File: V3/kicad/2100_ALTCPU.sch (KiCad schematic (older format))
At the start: 7 parts, among them J2100 Conn_02x20_Counter_Clockwise, U2100 Z8-L180-S180-180-PQFP-80, U2101 GAL16V8, X2100 14.7456 MHz

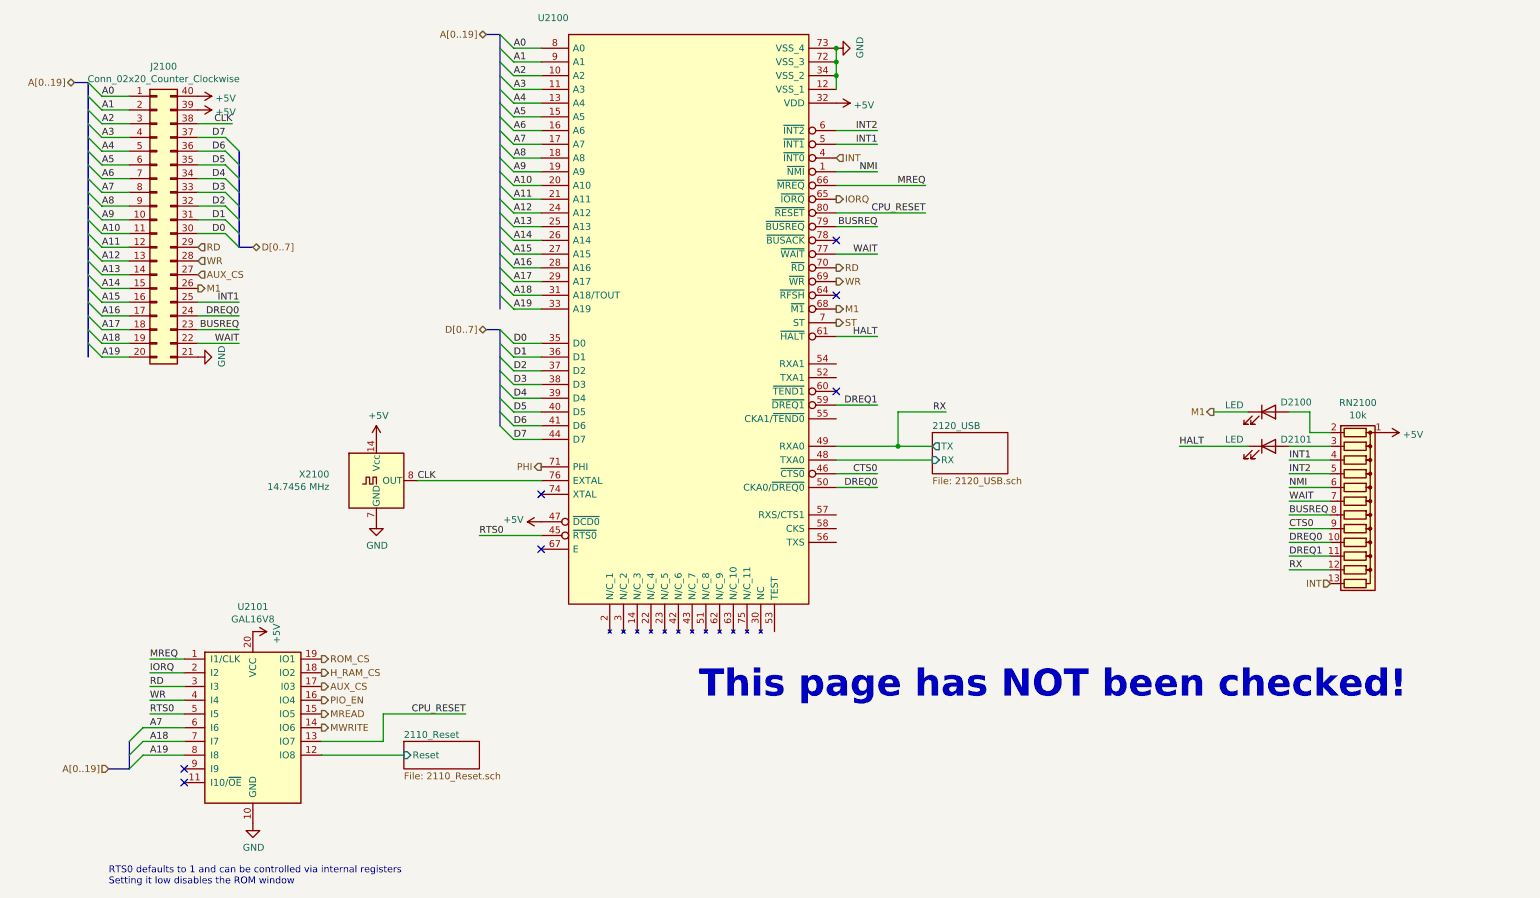
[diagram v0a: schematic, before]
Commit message: Fixed a few USB/UART issues
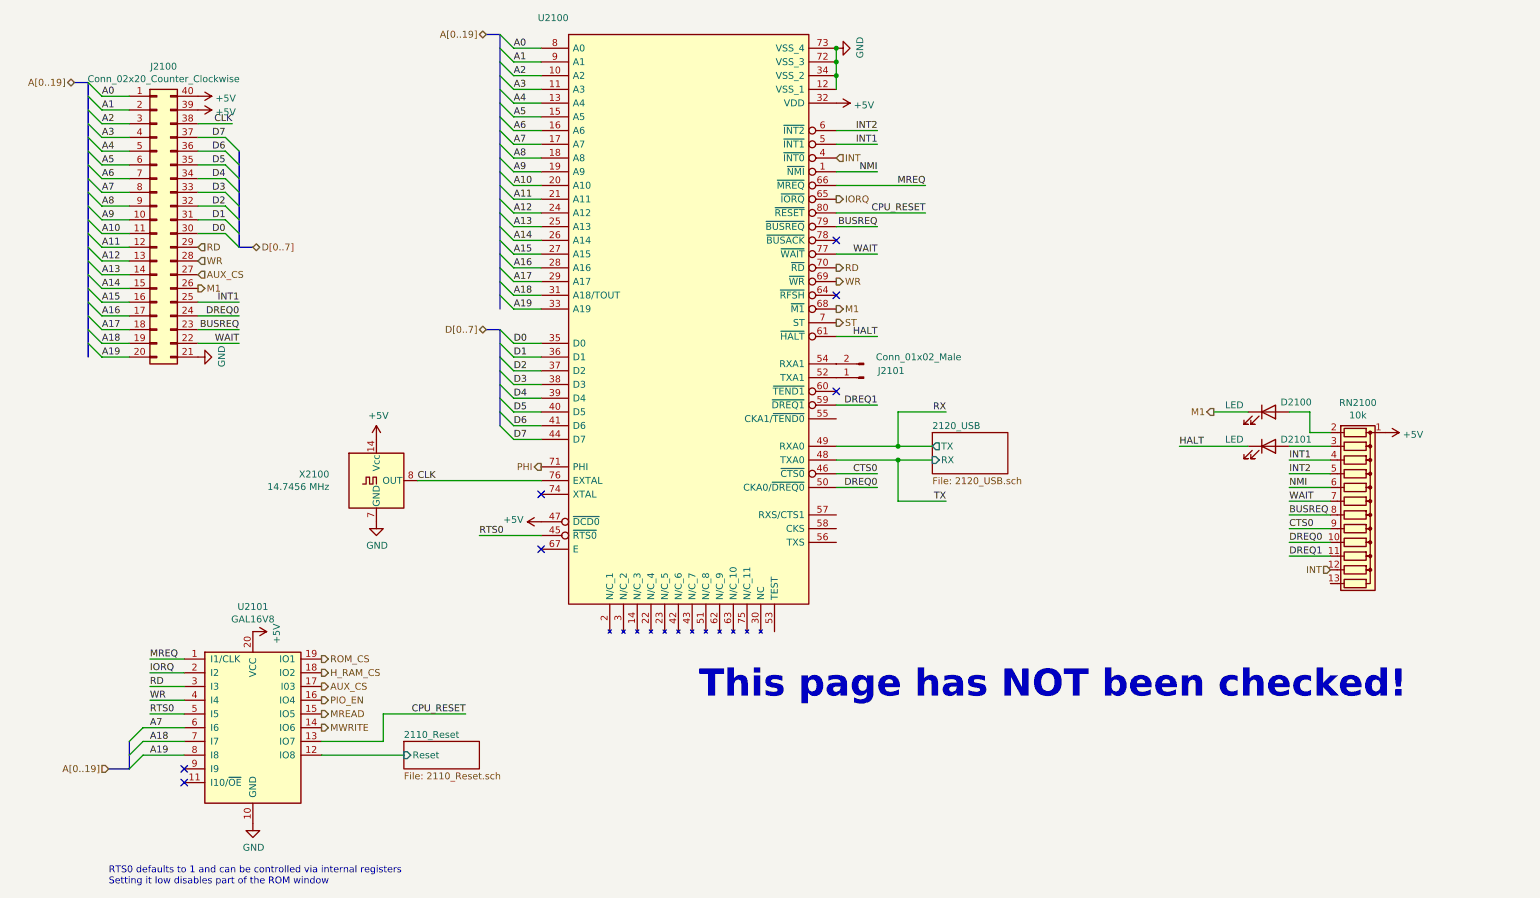
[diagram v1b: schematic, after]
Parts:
- added J2101: Conn_01x02_Male, Connector_PinHeader_2.54mm:PinHeader_1x02_P2.54mm_Vertical, symbol Connector:Conn_01x02_Male
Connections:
- net INT: now also RN2100.12 (R11); no longer RN2100.13 (R12)
- net RX: no longer RN2100.12 (R11)
- net at U2100.52 (TXA1): now also J2101.1 (Pin_1)
- net at U2100.54 (RXA1): now also J2101.2 (Pin_2)
- net 2120_USB/RX renamed TX
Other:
- note added: "RTS0 defaults to 1 and can be controlled via internal registers\nSetting it low disables part of the ROM window"
- note removed: "RTS0 defaults to 1 and can be controlled via internal registers\nSetting it low disables the ROM window"
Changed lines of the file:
@@
 Text HLabel 9500 4150 0    50   Output ~ 0
 M1
-Text HLabel 10350 5400 0    50   Input ~ 0
+Text HLabel 10350 5300 0    50   Input ~ 0
 INT
 NoConn ~ 6750 4000
@@
 	2000 6350 1750 6350
 Text Notes 1450 7600 0    50   ~ 0
-RTS0 defaults to 1 and can be controlled via internal registers\nSetting it low disables the ROM window
+RTS0 defaults to 1 and can be controlled via internal registers\nSetting it low disables part of the ROM window
 Wire Wire Line
 	3600 6650 3000 6650
@@
 	3700 4650 4600 4650
 Wire Wire Line
-	6750 4500 7450 4500
+	6750 4500 7200 4500
 NoConn ~ 2000 6750
 $Comp
@@
 Text Label 7550 4150 2    50   ~ 0
 RX
-Text Label 10050 5300 0    50   ~ 0
-RX
-Wire Wire Line
-	10350 5300 10050 5300
 Wire Wire Line
 	6750 4100 7050 4100
@@
 DREQ0
 $Comp
-L power:GND #PWR?
+L power:GND #PWR0140
 U 1 1 6275CB20
 P 2100 3750
-F 0 "#PWR?" H 2100 3500 50  0001 C CNN
+F 0 "#PWR0140" H 2100 3500 50  0001 C CNN
 F 1 "GND" H 2105 3577 50  0000 C CNN
 F 2 "" H 2100 3750 50  0001 C CNN
@@
 $EndComp
 $Comp
-L power:+5V #PWR?
+L power:+5V #PWR0142
 U 1 1 6275CB26
 P 2100 1850
-F 0 "#PWR?" H 2100 1700 50  0001 C CNN
+F 0 "#PWR0142" H 2100 1700 50  0001 C CNN
 F 1 "+5V" V 2115 1978 50  0000 L CNN
 F 2 "" H 2100 1850 50  0001 C CNN
@@
 $EndComp
 $Comp
-L power:+5V #PWR?
+L power:+5V #PWR0144
 U 1 1 627A29E2
 P 2100 1950
-F 0 "#PWR?" H 2100 1800 50  0001 C CNN
+F 0 "#PWR0144" H 2100 1800 50  0001 C CNN
 F 1 "+5V" V 2115 2078 50  0000 L CNN
 F 2 "" H 2100 1950 50  0001 C CNN
@@
 	0    1    1    0
 $EndComp
+Wire Wire Line
+	7200 4800 7550 4800
+Text Label 7550 4800 2    50   ~ 0
+TX
+Connection ~ 7200 4500
+Wire Wire Line
+	7200 4500 7450 4500
+Wire Wire Line
+	7200 4500 7200 4800
+$Comp
+L Connector:Conn_01x02_Male J?
+U 1 1 62765282
+P 6950 3900
+AR Path="/6191B6A2/61EBDADB/62542978/62765282" Ref="J?"  Part="1"
+AR Path="/6191B6A2/61EBDADB/62765282" Ref="J2101"  Part="1"
+F 0 "J2101" H 6750 3850 50  0000 C CNN
+F 1 "Conn_01x02_Male" H 6550 3750 50  0000 C CNN
+F 2 "Connector_PinHeader_2.54mm:PinHeader_1x02_P2.54mm_Vertical" H 6950 3900 50  0001 C CNN
+F 3 "~" H 6950 3900 50  0001 C CNN
+	1    6950 3900
+	-1   0    0    1
+$EndComp
 Wire Bus Line

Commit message: Still putting final touches on CPU page
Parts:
- removed J2100: Conn_02x20_Counter_Clockwise, Connector_PinSocket_2.54mm:PinSocket_2x20_P2.54mm_Vertical, symbol Connector_Generic:Conn_02x20_Counter_Clockwise
- removed RN2100: 10k, Resistor_THT:R_Array_SIP13, symbol Device:R_Network12
- added D2102: LED, LED_THT:LED_D3.0mm, symbol Device:LED
- added J2100: Conn_02x24_Counter_Clockwise, Connector_PinSocket_2.54mm:PinSocket_2x24_P2.54mm_Vertical, symbol Connector_Generic:Conn_02x24_Counter_Clockwise
- added RN2100: 10k, Resistor_THT:R_Array_SIP14, symbol Device:R_Network13
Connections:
- net +5V: now also J2100.23 (Pin_23), J2100.24 (Pin_24), RN2100.1 (common); no longer U2100.47 (~DCD0)
- net A0: now also J2100.1 (Pin_1)
- net A1: now also J2100.2 (Pin_2)
- net A10: now also J2100.11 (Pin_11)
- net A11: now also J2100.12 (Pin_12)
- net A12: now also J2100.13 (Pin_13)
- net A13: now also J2100.14 (Pin_14)
- net A14: now also J2100.15 (Pin_15)
- net A15: now also J2100.16 (Pin_16)
- net A16: now also J2100.17 (Pin_17)
- net A17: now also J2100.18 (Pin_18)
- net A18: now also J2100.19 (Pin_19)
- net A19: now also J2100.20 (Pin_20)
- net A2: now also J2100.3 (Pin_3)
- net A3: now also J2100.4 (Pin_4)
- net A4: now also J2100.5 (Pin_5)
- net A5: now also J2100.6 (Pin_6)
- net A6: now also J2100.7 (Pin_7)
- net A7: now also J2100.8 (Pin_8)
- net A8: now also J2100.9 (Pin_9)
- net A9: now also J2100.10 (Pin_10)
- net AUX_CS: now also J2100.38 (Pin_38)
- net BUSREQ: now also J2100.32 (Pin_32), RN2100.10 (R9)
- net CTS0: now also RN2100.11 (R10)
- net D0: now also J2100.41 (Pin_41)
- net D1: now also J2100.42 (Pin_42)
- net D2: now also J2100.43 (Pin_43)
- net D3: now also J2100.44 (Pin_44)
- net D4: now also J2100.45 (Pin_45)
- net D5: now also J2100.46 (Pin_46)
- net D6: now also J2100.47 (Pin_47)
- net D7: now also J2100.48 (Pin_48)
- net DREQ0: now also J2100.33 (Pin_33); no longer U2100.50 (CKA0/~DREQ0)
- net DREQ1: now also RN2100.13 (R12)
- net GND: now also D2102.1 (K), J2100.25 (Pin_25), J2100.26 (Pin_26)
- net INT: now also RN2100.5 (R4)
- net INT1: now also J2100.34 (Pin_34), RN2100.6 (R5)
- net INT2: now also RN2100.7 (R6)
- net IORQ: now also J2100.30 (Pin_30)
- net M1: now also J2100.40 (Pin_40)
- net MREQ: now also J2100.29 (Pin_29)
- net NMI: now also RN2100.8 (R7)
- net PHI: now also J2100.39 (Pin_39)
- net RD: now also J2100.35 (Pin_35)
- net RTS0: now also J2100.28 (Pin_28)
- net WAIT: now also J2100.31 (Pin_31), RN2100.9 (R8)
- net WR: now also J2100.36 (Pin_36)
- net RXS: now reaches U2100.57 (RXS/CTS1)
- net RXS: now also RN2100.12 (R11)
- net at D2101.2 (A): now also RN2100.3 (R2)
- net at D2100.2 (A): now also RN2100.2 (R1)
- net CPU_RESET renamed C_RST
- net C_RST: now also J2100.27 (Pin_27)
- net ST: no longer names the net of U2100.7 (ST)
- new net: D2102.2 (A), RN2100.4 (R3)
- new net DCD0: RN2100.14 (R13), U2100.47 (~DCD0)
- no-connect marks 7 -> 13
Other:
- note added: "Tie CKS high?"
- moved on the sheet: D2100, D2101

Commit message: Hopefully the last major changes to the CPU
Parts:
- removed D2102: LED, LED_THT:LED_D3.0mm, symbol Device:LED
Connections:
- net 2110_Reset/Reset: now also U2101.9 (I9); no longer U2101.12 (IO8)
- net AUX_CS: now also J2100.21 (Pin_21); no longer J2100.38 (Pin_38)
- net BUSREQ: now also RN2100.9 (R8); no longer RN2100.10 (R9)
- net CTS0: now also RN2100.10 (R9); no longer RN2100.11 (R10)
- net C_RST: now also U2101.12 (IO8); no longer U2101.13 (IO7)
- net DCD0: now also RN2100.13 (R12); no longer RN2100.14 (R13)
- net DREQ1: now also RN2100.12 (R11); no longer RN2100.13 (R12)
- net INT: now also RN2100.4 (R3); no longer RN2100.5 (R4)
- net INT1: now also RN2100.5 (R4); no longer RN2100.6 (R5)
- net INT2: now also RN2100.6 (R5); no longer RN2100.7 (R6)
- net M1: now also J2100.37 (Pin_37); no longer J2100.40 (Pin_40)
- net NMI: now also RN2100.7 (R6); no longer RN2100.8 (R7)
- net PHI: now also J2100.38 (Pin_38); no longer J2100.39 (Pin_39)
- net RXS: now also RN2100.11 (R10); no longer RN2100.12 (R11), U2100.57 (RXS/CTS1)
- net WAIT: now also RN2100.8 (R7); no longer RN2100.9 (R8)
- net CKS: now reaches U2100.58 (CKS)
- net CKS: now also RN2100.14 (R13)
- net BUSACK: now reaches U2100.78 (~BUSACK)
- net BUSACK: now also J2100.39 (Pin_39)
- no-connect marks 13 -> 11
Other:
- note removed: "Tie CKS high?"
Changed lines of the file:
@@
 Wire Wire Line
 	6750 1600 6750 1700
-Text HLabel 4600 4550 0    50   Output ~ 0
-PHI
-NoConn ~ 6750 2900
 Text Label 4400 1500 0    50   ~ 0
 A0
@@
 $EndComp
 Entry Wire Line
-	1600 6750 1700 6650
+	1700 6650 1600 6550
 Wire Wire Line
 	1700 6450 2000 6450
@@
 A18
 Wire Bus Line
-	1600 6750 1450 6750
-Text HLabel 1450 6750 0    50   Input ~ 0
+	1600 6350 1450 6350
+Text HLabel 1450 6350 0    50   Input ~ 0
 A[0..19]
 $Comp
@@
 ROM_CS
 Entry Wire Line
-	1600 6650 1700 6550
-Entry Wire Line
-	1600 6550 1700 6450
+	1700 6550 1600 6450
+Entry Wire Line
+	1700 6450 1600 6350
 Wire Wire Line
 	1700 6650 2000 6650
@@
 D[0..7]
 $Sheet
-S 3600 6550 550  200
+S 850  6650 550  200
 U 62512FB8
 F0 "2110_Reset" 50
 F1 "2110_Reset.sch" 50
-F2 "Reset" I L 3600 6650 50
+F2 "Reset" I R 1400 6750 50
 $EndSheet
 $Sheet
@@
 Text Label 7050 2500 2    50   ~ 0
 MREQ
-Text Label 4300 5050 0    50   ~ 0
-RTS0
 Text Label 1750 6350 0    50   ~ 0
 RTS0
@@
 RTS0 defaults to 1 and can be controlled via internal registers\nSetting it low disables part of the ROM window
 Wire Wire Line
-	3600 6650 3000 6650
-Wire Wire Line
-	3000 6550 3450 6550
-Wire Wire Line
-	3450 6550 3450 6350
-Wire Wire Line
-	3450 6350 4050 6350
-Text Label 4050 6350 2    50   ~ 0
-C_RST
+	1400 6750 2000 6750
 Wire Wire Line
 	3700 4650 4600 4650
 Wire Wire Line
 	6750 4500 7200 4500
-NoConn ~ 2000 6750
 $Comp
 L Logic_Programmable:GAL16V8 U?
@@
 $EndComp
 NoConn ~ 2000 6850
-Text HLabel 2100 2850 2    50   Input ~ 0
+Text HLabel 1600 3850 0    50   Input ~ 0
 AUX_CS
 Wire Wire Line
@@
 INT1
 Wire Wire Line
-	10350 4800 10050 4800
-Wire Wire Line
 	10350 4700 10050 4700
-Text Label 10050 4800 0    50   ~ 0
+Wire Wire Line
+	10350 4600 10050 4600
+Text Label 10050 4700 0    50   ~ 0
 INT2
-Text Label 10050 4700 0    50   ~ 0
+Text Label 10050 4600 0    50   ~ 0
 INT1
 Wire Wire Line
@@
 NMI
 Wire Wire Line
-	10350 4900 10050 4900
-Text Label 10050 4900 0    50   ~ 0
+	10350 4800 10050 4800
+Text Label 10050 4800 0    50   ~ 0
 NMI
 Wire Wire Line
@@
 WAIT
 Wire Wire Line
-	10350 5100 10050 5100
-Text Label 10050 5100 0    50   ~ 0
-BUSREQ
-Wire Wire Line
 	10350 5000 10050 5000
 Text Label 10050 5000 0    50   ~ 0
+BUSREQ
+Wire Wire Line
+	10350 4900 10050 4900
+Text Label 10050 4900 0    50   ~ 0
 WAIT
 Wire Wire Line
@@
 CTS0
 Wire Wire Line
-	10350 5200 10050 5200
-Text Label 10050 5200 0    50   ~ 0
+	10350 5100 10050 5100
+Text Label 10050 5100 0    50   ~ 0
 CTS0
 Wire Wire Line
-	10350 5400 10050 5400
-Text Label 10050 5400 0    50   ~ 0
+	10350 5300 10050 5300
+Text Label 10050 5300 0    50   ~ 0
 DREQ1
-Text HLabel 2100 2650 2    50   Output ~ 0
-M1
 Wire Wire Line
 	2100 3250 2400 3250
@@
 $EndComp
 Wire Wire Line
-	10350 4500 9950 4500
-Wire Wire Line
-	9950 4500 9950 4650
-Wire Wire Line
-	9950 4650 9750 4650
-Wire Wire Line
 	9950 4300 10350 4300
 Wire Wire Line
@@
 Wire Wire Line
 	9750 4150 9950 4150
-$Comp
-L Device:LED D2102
-U 1 1 627D5172
-P 9600 4650
-F 0 "D2102" H 9800 4750 50  0000 C TNN
-F 1 "LED" H 9350 4700 50  0000 C CNN
-F 2 "LED_THT:LED_D3.0mm" H 9600 4650 50  0001 C CNN
-F 3 "~" H 9600 4650 50  0001 C CNN
-	1    9600 4650
-	1    0    0    -1
-$EndComp
-Wire Wire Line
-	9200 4650 9450 4650
-$Comp
-L power:GND #PWR?
-U 1 1 627DB26E
-P 9200 4650
-F 0 "#PWR?" H 9200 4400 50  0001 C CNN
-F 1 "GND" V 9205 4522 50  0000 R CNN
-F 2 "" H 9200 4650 50  0001 C CNN
-F 3 "" H 9200 4650 50  0001 C CNN
-	1    9200 4650
-	0    1    1    0
-$EndComp
-Text HLabel 2100 2750 2    50   Output ~ 0
-PHI
 $Comp
 L Connector_Generic:Conn_02x24_Counter_Clockwise J2100
@@
 Entry Wire Line
 	2300 2550 2400 2450
-Text HLabel 1750 6150 0    50   Output ~ 0
-RD
-Text HLabel 1750 6250 0    50   Output ~ 0
-WR
 Wire Wire Line
 	2100 3650 2350 3650
@@
 M1
 Wire Wire Line
-	10350 4600 10050 4600
-Text Label 10050 4600 0    50   ~ 0
+	10350 4500 10050 4500
+Text Label 10050 4500 0    50   ~ 0
 INT0
 Wire Wire Line
@@
 DCD0
 Wire Wire Line
-	4300 5050 4600 5050
-Wire Wire Line
-	10350 5500 10050 5500
-Text Label 10050 5500 0    50   ~ 0
+	10350 5400 10050 5400
+Text Label 10050 5400 0    50   ~ 0
 DCD0
 NoConn ~ 6300 5750
@@
 	0    1    1    0
 $EndComp
-NoConn ~ 6750 5000
 NoConn ~ 6750 5100
 NoConn ~ 6750 4200
 NoConn ~ 6750 4700
 Wire Wire Line
-	6750 4900 7050 4900
-Text Label 7050 4900 2    50   ~ 0
+	10350 5200 10050 5200
+Text Label 10050 5200 0    50   ~ 0
 RXS
 Wire Wire Line
-	10350 5300 10050 5300
-Text Label 10050 5300 0    50   ~ 0
-RXS
+	10350 5500 10050 5500
+Text Label 10050 5500 0    50   ~ 0
+CKS
+NoConn ~ 6750 4900
+Wire Wire Line
+	6750 5000 7050 5000
+Text Label 7050 5000 2    50   ~ 0
+CKS
+Text Label 2350 2950 2    50   ~ 0
+M1
+Wire Wire Line
+	2100 2950 2350 2950
+Wire Wire Line
+	2100 2850 2350 2850
+Text Label 2350 2850 2    50   ~ 0
+PHI
+Text HLabel 4300 4550 0    50   Output ~ 0
+PHI
+Wire Wire Line
+	4300 5050 4600 5050
+Text Label 4300 5050 0    50   ~ 0
+RTS0
+Wire Wire Line
+	4300 4550 4600 4550
+Text Label 4300 4550 0    50   ~ 0
+PHI
+Text Label 3300 6650 2    50   ~ 0
+C_RST
+Wire Wire Line
+	3000 6650 3300 6650
+Wire Wire Line
+	6750 2900 7050 2900
+Text Label 7050 2900 2    50   ~ 0
+BUSACK
+Wire Wire Line
+	2100 2750 2400 2750
+Text Label 2400 2750 2    50   ~ 0
+BUSACK
 Wire Bus Line
-	1600 6550 1600 6750
+	1600 6350 1600 6550
 Wire Bus Line
 	4300 3550 4300 4250
@@
 Wire Bus Line
 	4300 1400 4300 3400
-Text Notes 7200 5150 0    50   ~ 0
-Tie CKS high?
 $EndSCHEMATC
